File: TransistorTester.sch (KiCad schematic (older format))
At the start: 18 parts, among them IC1 ATMEGA8-P, J1 TEST POINTS, J2 POWER, U2 78L05

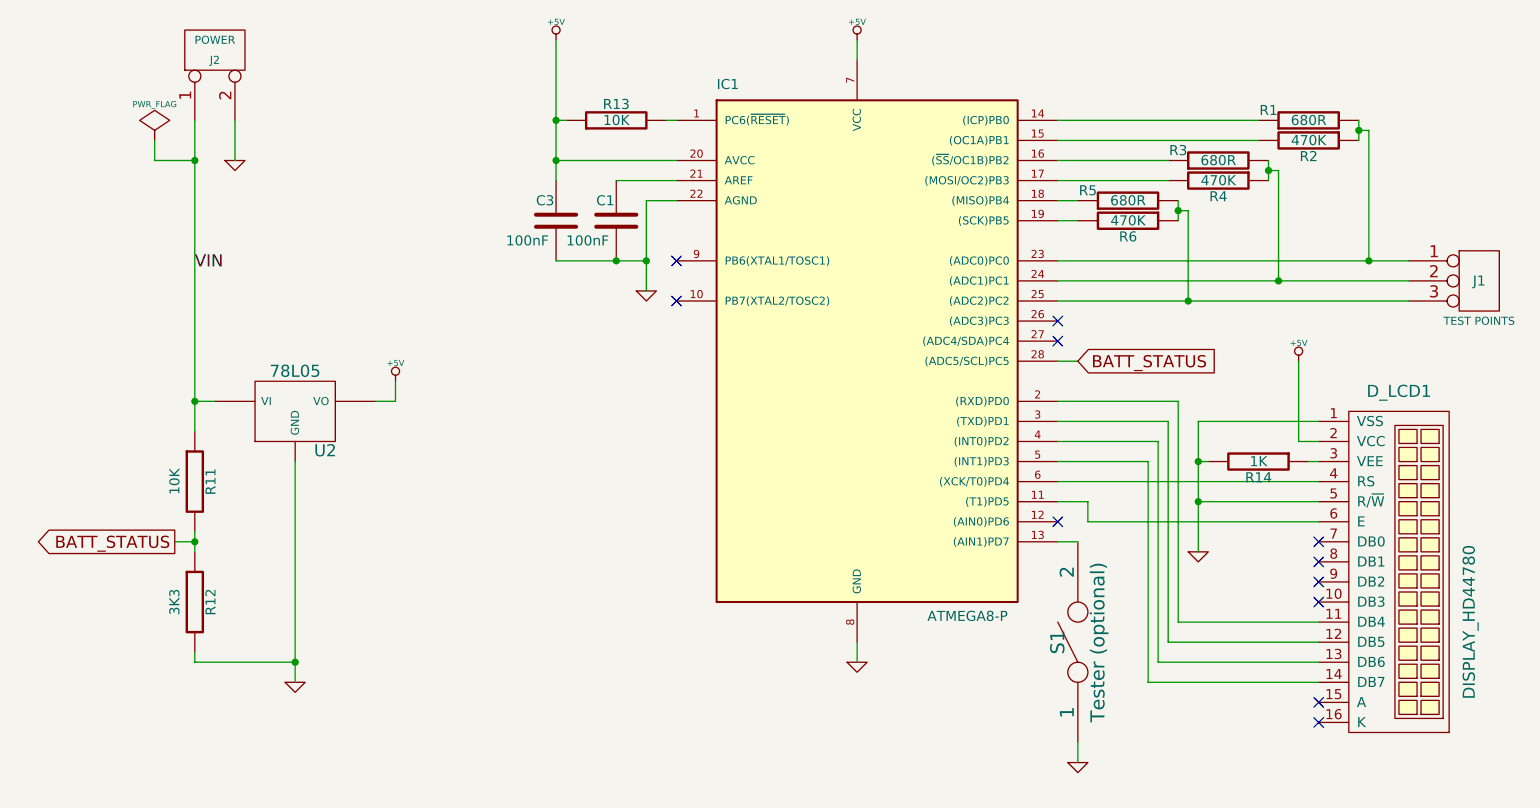
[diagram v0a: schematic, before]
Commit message: v.0.3: LCD; Wired backlit; TO-220 LM7805
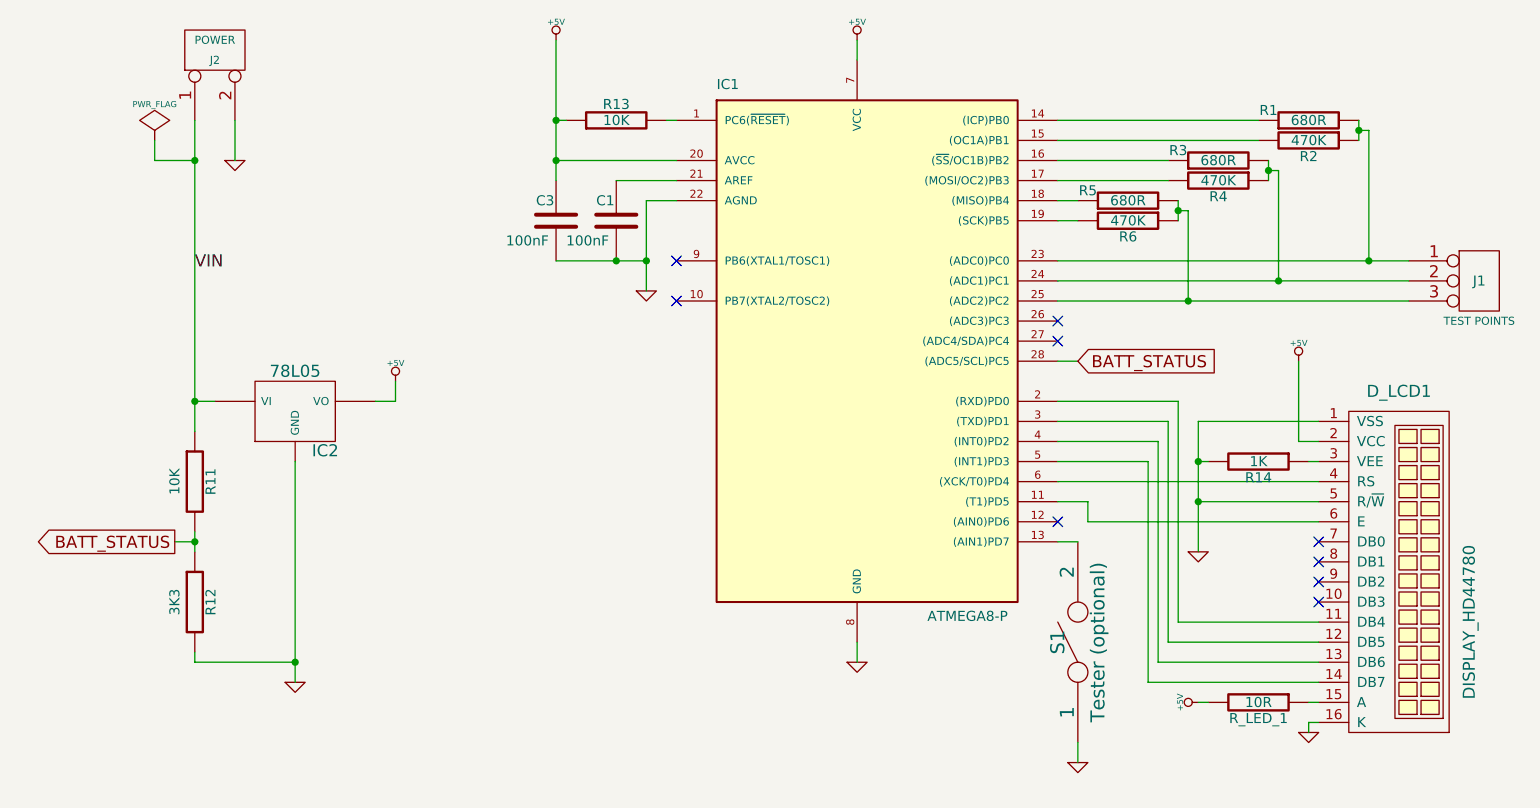
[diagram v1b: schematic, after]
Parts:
- added R_LED_1: 10R, R5, symbol R
- renumbered U2 to IC2
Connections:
- net +5V: now also R_LED_1.2
- net GND: now also D_LCD1.16 (K)
- net at D_LCD1.15 (A): now also R_LED_1.1
- no-connect marks 11 -> 9
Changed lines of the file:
@@
-EESchema Schematic File Version 2  date 19/02/2012 11:03:57
+EESchema Schematic File Version 2  date 19/02/2012 18:02:46
 LIBS:power
 LIBS:device
@@
 Sheet 1 1
 Title "AVR Transistor Tester"
-Date "18 feb 2012"
-Rev "0.2"
+Date "19 feb 2012"
+Rev "0.3"
 Comp ""
 Comment1 "Drawn by Dimitar Kovachev"
@@
 VIN
 Wire Wire Line
+	6500 5000 6450 5000
+Wire Wire Line
+	7000 5150 7000 5100
+Wire Wire Line
+	7000 5100 7050 5100
+Wire Wire Line
+	7050 5000 7000 5000
+Wire Wire Line
 	1450 3650 1450 2100
 Wire Wire Line
@@
 	5750 3300 5850 3300
 $Comp
-L GND #PWR?
+L GND #PWR01
 U 1 1 4F3FC649
 P 1650 2300
-F 0 "#PWR?" H 1650 2300 30  0001 C CNN
+F 0 "#PWR01" H 1650 2300 30  0001 C CNN
 F 1 "GND" H 1650 2230 30  0001 C CNN
 	1    1650 2300
@@
 	1    0    0    -1
 $EndComp
-NoConn ~ 7050 5100
-NoConn ~ 7050 5000
 NoConn ~ 7050 4500
 NoConn ~ 7050 4400
@@
 $EndComp
 $Comp
-L 78L05 U2
+L 78L05 IC2
 U 1 1 4F3C0AE5
 P 1950 3550
-F 0 "U2" H 2100 3354 60  0000 C CNN
+F 0 "IC2" H 2100 3354 60  0000 C CNN
 F 1 "78L05" H 1950 3750 60  0000 C CNN
 	1    1950 3550
@@
 	1    0    0    -1
 $EndComp
+$Comp
+L GND #PWR012
+U 1 1 4F41114D
+P 7000 5150
+F 0 "#PWR012" H 7000 5150 30  0001 C CNN
+F 1 "GND" H 7000 5080 30  0001 C CNN
+	1    7000 5150
+	1    0    0    -1
+$EndComp
+$Comp
+L +5V #PWR013
+U 1 1 4F411164
+P 6450 5000
+F 0 "#PWR013" H 6450 5090 20  0001 C CNN
+F 1 "+5V" H 6450 5090 30  0000 C CNN
+	1    6450 5000
+	0    -1   -1   0
+$EndComp
+$Comp
+L R R_LED_1
+U 1 1 4F411152
+P 6750 5000
+F 0 "R_LED_1" V 6830 5000 50  0000 C CNN
+F 1 "10R" V 6750 5000 50  0000 C CNN
+F 2 "R5" H 6750 5000 60  0001 C CNN
+	1    6750 5000
+	0    1    1    0
+$EndComp
 $EndSCHEMATC

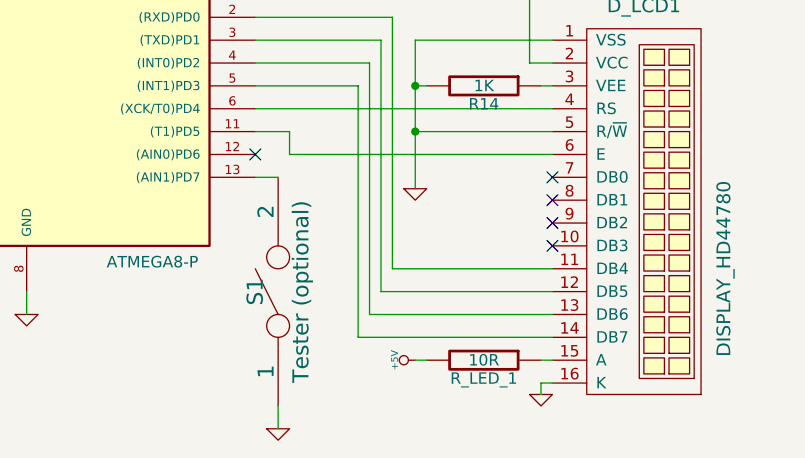
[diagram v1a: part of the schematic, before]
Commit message: v.0.4 Add V-Button; PCB resize; Fixes
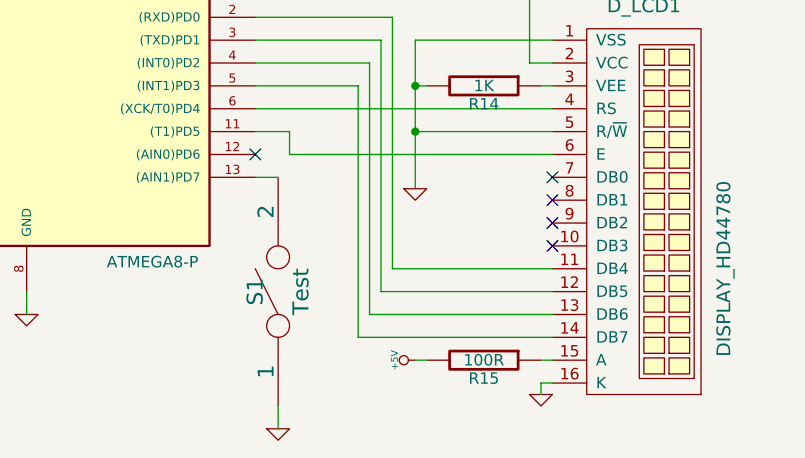
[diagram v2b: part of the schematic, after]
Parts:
- R15: renamed from R_LED_1; value 10R -> 100R
- S1: value Tester (optional) -> Test
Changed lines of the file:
@@
 Sheet 1 1
 Title "AVR Transistor Tester"
-Date "19 feb 2012"
-Rev "0.3"
+Date "26 feb 2012"
+Rev "0.4"
 Comp ""
-Comment1 "Drawn by Dimitar Kovachev"
-Comment2 "Designed by Markus Frejek http://www.mikrocontroller.net/articles/AVR-Transistortester"
-Comment3 ""
+Comment1 "Schematic and PCB design by Dimitar Kovachev"
+Comment2 "http://www.mikrocontroller.net/articles/AVR-Transistortester"
+Comment3 "Original design by Markus Frejek "
 Comment4 ""
 $EndDescr
@@
 P 5850 4700
 F 0 "S1" H 5850 4800 70  0000 C CNN
-F 1 "Tester (optional)" H 5850 4600 70  0000 C CNN
+F 1 "Test" H 5850 4600 70  0000 C CNN
 	1    5850 4700
 	0    -1   -1   0
@@
 $EndComp
 $Comp
-L R R_LED_1
+L R R15
 U 1 1 4F411152
 P 6750 5000
-F 0 "R_LED_1" V 6830 5000 50  0000 C CNN
-F 1 "10R" V 6750 5000 50  0000 C CNN
+F 0 "R15" V 6830 5000 50  0000 C CNN
+F 1 "100R" V 6750 5000 50  0000 C CNN
 F 2 "R5" H 6750 5000 60  0001 C CNN
 	1    6750 5000

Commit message: Updated to latest libs
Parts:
- removed D_LCD1: DISPLAY_HD44780, symbol DISPLAY_HD44780
- added D_LCD1: LV_1602_LCD_HD44780, symbol LV_1602_LCD_HD44780
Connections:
- net +5V: now also D_LCD1.2 (VCC)
- net GND: now also D_LCD1.1 (VSS), D_LCD1.16 (K), D_LCD1.5 (R/~W)
- net at IC1.11 ((T1)PD5): now also D_LCD1.6 (E)
- net at IC1.2 ((RXD)PD0): now also D_LCD1.11 (DB4)
- net at IC1.3 ((TXD)PD1): now also D_LCD1.12 (DB5)
- net at IC1.4 ((INT0)PD2): now also D_LCD1.13 (DB6)
- net at IC1.5 ((INT1)PD3): now also D_LCD1.14 (DB7)
- net at IC1.6 ((XCK/T0)PD4): now also D_LCD1.4 (RS)
- net at R15.1: now also D_LCD1.15 (A)
- net at R14.1: now also D_LCD1.3 (CON)
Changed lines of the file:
@@
 LIBS:contrib
 LIBS:valves
-LIBS:display_lcd
+LIBS:lowvoltage
 LIBS:TransistorTester-cache
 EELAYER 25  0
@@
 $EndComp
 $Comp
-L DISPLAY_HD44780 D_LCD1
-U 1 1 4F3BE52C
+L LV_1602_LCD_HD44780 D_LCD1
+U 1 1 4F53BDBA
 P 7400 4350
 F 0 "D_LCD1" V 8300 4400 60  0000 C CNN
-F 1 "DISPLAY_HD44780" H 7150 4750 60  0000 C CNN
+F 1 "LV_1602_LCD_HD44780" H 7150 4750 60  0000 C CNN
 	1    7400 4350
 	0    1    -1   0

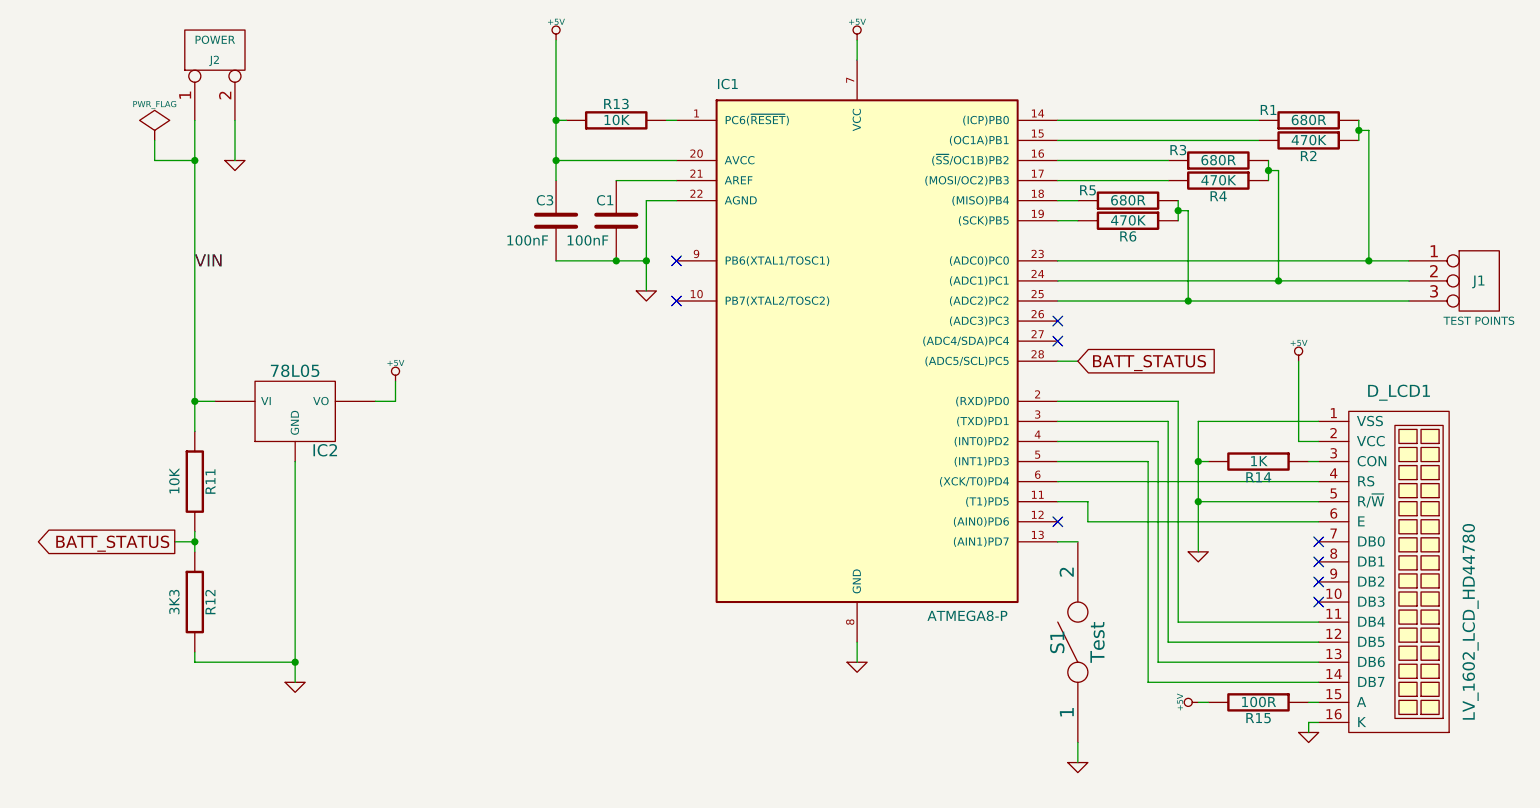
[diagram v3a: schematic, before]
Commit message: Added protection diode, VReg caps, button pull-up
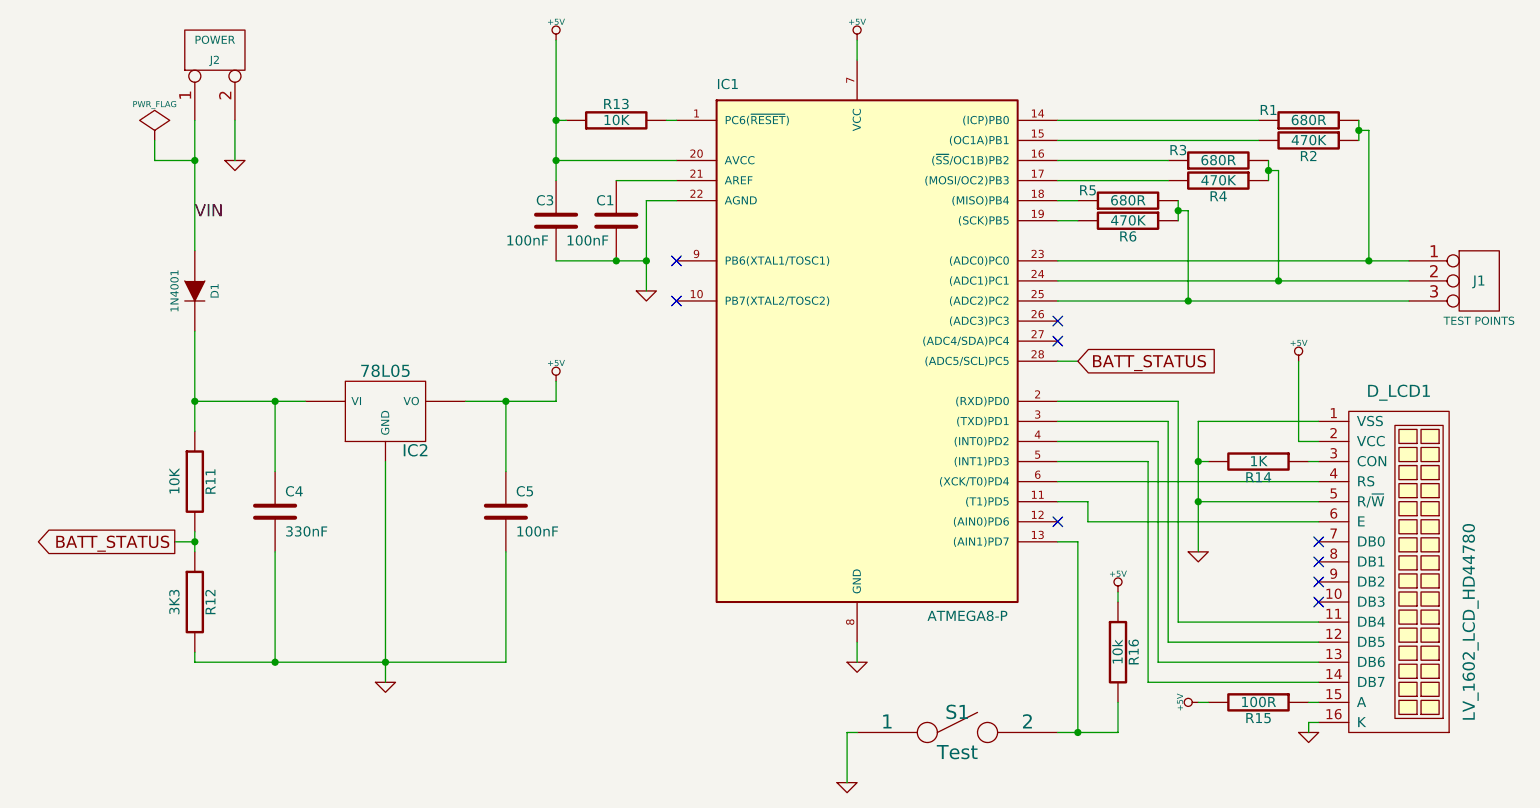
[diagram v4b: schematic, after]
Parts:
- added C4: 330nF, symbol C
- added C5: 100nF, symbol C
- added D1: 1N4001, symbol DIODE
- added R16: 10k, symbol R
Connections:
- net +5V: now also C5.1, R16.1
- net GND: now also C4.2, C5.2
- net VIN: now also D1.1 (A); no longer IC2.VI, R11.1
- net at IC1.13 ((AIN1)PD7), S1.2: now also R16.2
- new net: C4.1, D1.2 (K), IC2.VI, R11.1
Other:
- moved on the sheet: IC2, S1
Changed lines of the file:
@@
-EESchema Schematic File Version 2  date 19/02/2012 18:02:46
+EESchema Schematic File Version 2  date Mon 09 Jul 2012 10:21:46 PM EEST
 LIBS:power
 LIBS:device
@@
 EELAYER 25  0
 EELAYER END
-$Descr A4 11700 8267
+$Descr A4 11693 8268
 encoding utf-8
 Sheet 1 1
 Title "AVR Transistor Tester"
-Date "26 feb 2012"
-Rev "0.4"
+Date "9 jul 2012"
+Rev "0.5"
 Comp ""
 Comment1 "Schematic and PCB design by Dimitar Kovachev"
@@
 Comment4 ""
 $EndDescr
-Text Label 1450 2850 0    60   ~ 0
+Text Label 1450 2600 0    60   ~ 0
 VIN
 Wire Wire Line
@@
 	7050 5000 7000 5000
 Wire Wire Line
-	1450 3650 1450 2100
+	1450 3150 1450 3650
 Wire Wire Line
 	1650 2300 1650 2100
@@
 	1350 4200 1450 4200
 Wire Wire Line
-	1450 4250 1450 4150
+	1450 4150 1450 4250
 Wire Wire Line
 	6500 3800 6450 3800
 Wire Wire Line
-	1550 3500 1450 3500
+	1450 3500 2000 3500
 Wire Wire Line
 	5750 3900 7050 3900
@@
 	7050 3600 6450 3600
 Wire Wire Line
-	1950 4900 1950 3800
+	2400 3800 2400 4900
 Wire Wire Line
 	3300 2100 3250 2100
-Wire Wire Line
-	5850 5300 5850 5200
 Connection ~ 3250 2300
 Wire Wire Line
@@
 Connection ~ 6850 2900
 Wire Wire Line
-	7500 2900 5750 2900
+	5750 2900 7500 2900
 Wire Wire Line
 	7300 2800 7300 2150
@@
 	6750 2200 5750 2200
 Wire Wire Line
-	7500 2800 5750 2800
+	5750 2800 7500 2800
 Connection ~ 7300 2800
 Wire Wire Line
-	7500 3000 5750 3000
+	5750 3000 7500 3000
 Connection ~ 6400 3000
 Wire Wire Line
@@
 	4750 4700 4750 4800
 Wire Wire Line
-	3700 2800 3250 2800
+	3250 2800 3700 2800
 Connection ~ 3550 2800
 Wire Wire Line
@@
 	3800 2100 3850 2100
 Wire Wire Line
-	2350 3500 2450 3500
-Wire Wire Line
-	2450 3500 2450 3400
+	2800 3500 3250 3500
+Wire Wire Line
+	3250 3500 3250 3400
 Wire Wire Line
 	7050 4000 6450 4000
@@
 	1450 4750 1450 4800
 Wire Wire Line
-	1450 4800 1950 4800
-Connection ~ 1950 4800
+	1450 4800 3000 4800
+Connection ~ 2400 4800
 Connection ~ 1450 3500
 Wire Wire Line
@@
 L GND #PWR03
 U 1 1 4F3C0B02
-P 1950 4900
-F 0 "#PWR03" H 1950 4900 30  0001 C CNN
-F 1 "GND" H 1950 4830 30  0001 C CNN
-	1    1950 4900
+P 2400 4900
+F 0 "#PWR03" H 2400 4900 30  0001 C CNN
+F 1 "GND" H 2400 4830 30  0001 C CNN
+	1    2400 4900
 	1    0    0    -1
 $EndComp
@@
 L +5V #PWR04
 U 1 1 4F3C0AFC
-P 2450 3400
-F 0 "#PWR04" H 2450 3490 20  0001 C CNN
-F 1 "+5V" H 2450 3490 30  0000 C CNN
-	1    2450 3400
+P 3250 3400
+F 0 "#PWR04" H 3250 3490 20  0001 C CNN
+F 1 "+5V" H 3250 3490 30  0000 C CNN
+	1    3250 3400
 	1    0    0    -1
 $EndComp
@@
 L 78L05 IC2
 U 1 1 4F3C0AE5
-P 1950 3550
-F 0 "IC2" H 2100 3354 60  0000 C CNN
-F 1 "78L05" H 1950 3750 60  0000 C CNN
-	1    1950 3550
+P 2400 3550
+F 0 "IC2" H 2550 3354 60  0000 C CNN
+F 1 "78L05" H 2400 3750 60  0000 C CNN
+	1    2400 3550
 	1    0    0    -1
 $EndComp
@@
 L GND #PWR05
 U 1 1 4F3C0A04
-P 5850 5300
-F 0 "#PWR05" H 5850 5300 30  0001 C CNN
-F 1 "GND" H 5850 5230 30  0001 C CNN
-	1    5850 5300
+P 4700 5400
+F 0 "#PWR05" H 4700 5400 30  0001 C CNN
+F 1 "GND" H 4700 5330 30  0001 C CNN
+	1    4700 5400
 	1    0    0    -1
 $EndComp
@@
 L SPST S1
 U 1 1 4F3C09DA
-P 5850 4700
-F 0 "S1" H 5850 4800 70  0000 C CNN
-F 1 "Test" H 5850 4600 70  0000 C CNN
-	1    5850 4700
-	0    -1   -1   0
+P 5250 5150
+F 0 "S1" H 5250 5250 70  0000 C CNN
+F 1 "Test" H 5250 5050 70  0000 C CNN
+	1    5250 5150
+	1    0    0    -1
 $EndComp
 $Comp
@@
 	0    1    1    0
 $EndComp
+$Comp
+L C C4
+U 1 1 4FFB2D64
+P 1850 4050
+F 0 "C4" H 1900 4150 50  0000 L CNN
+F 1 "330nF" H 1900 3950 50  0000 L CNN
+	1    1850 4050
+	1    0    0    -1
+$EndComp
+$Comp
+L C C5
+U 1 1 4FFB2D71
+P 3000 4050
+F 0 "C5" H 3050 4150 50  0000 L CNN
+F 1 "100nF" H 3050 3950 50  0000 L CNN
+	1    3000 4050
+	1    0    0    -1
+$EndComp
+Wire Wire Line
+	1850 3500 1850 3850
+Connection ~ 1850 3500
+Wire Wire Line
+	1850 4250 1850 4800
+Connection ~ 1850 4800
+Wire Wire Line
+	3000 3500 3000 3850
+Connection ~ 3000 3500
+Wire Wire Line
+	3000 4800 3000 4250
+$Comp
+L DIODE D1
+U 1 1 4FFB2F14
+P 1450 2950
+F 0 "D1" H 1450 3050 40  0000 C CNN
+F 1 "1N4001" H 1450 2850 40  0000 C CNN
+	1    1450 2950
+	0    1    1    0
+$EndComp
+Wire Wire Line
+	1450 2100 1450 2750
+$Comp
+L R R16
+U 1 1 4FFB3056
+P 6050 4750
+F 0 "R16" V 6130 4750 50  0000 C CNN
+F 1 "10k" V 6050 4750 50  0000 C CNN
+	1    6050 4750
+	1    0    0    -1
+$EndComp
+$Comp
+L +5V #PWR014
+U 1 1 4FFB3063
+P 6050 4450
+F 0 "#PWR014" H 6050 4540 20  0001 C CNN
+F 1 "+5V" H 6050 4540 30  0000 C CNN
+	1    6050 4450
+	1    0    0    -1
+$EndComp
+Wire Wire Line
+	6050 4450 6050 4500
+Wire Wire Line
+	4750 5150 4700 5150
+Wire Wire Line
+	4700 5150 4700 5400
+Wire Wire Line
+	5850 4200 5850 5150
+Wire Wire Line
+	5750 5150 6050 5150
+Wire Wire Line
+	6050 5150 6050 5000
+Connection ~ 5850 5150
 $EndSCHEMATC
